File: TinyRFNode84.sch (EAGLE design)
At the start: 13 parts, among them IC3 MCP1703CB, T1 2N2222, U1 ATTINY84-20SSU

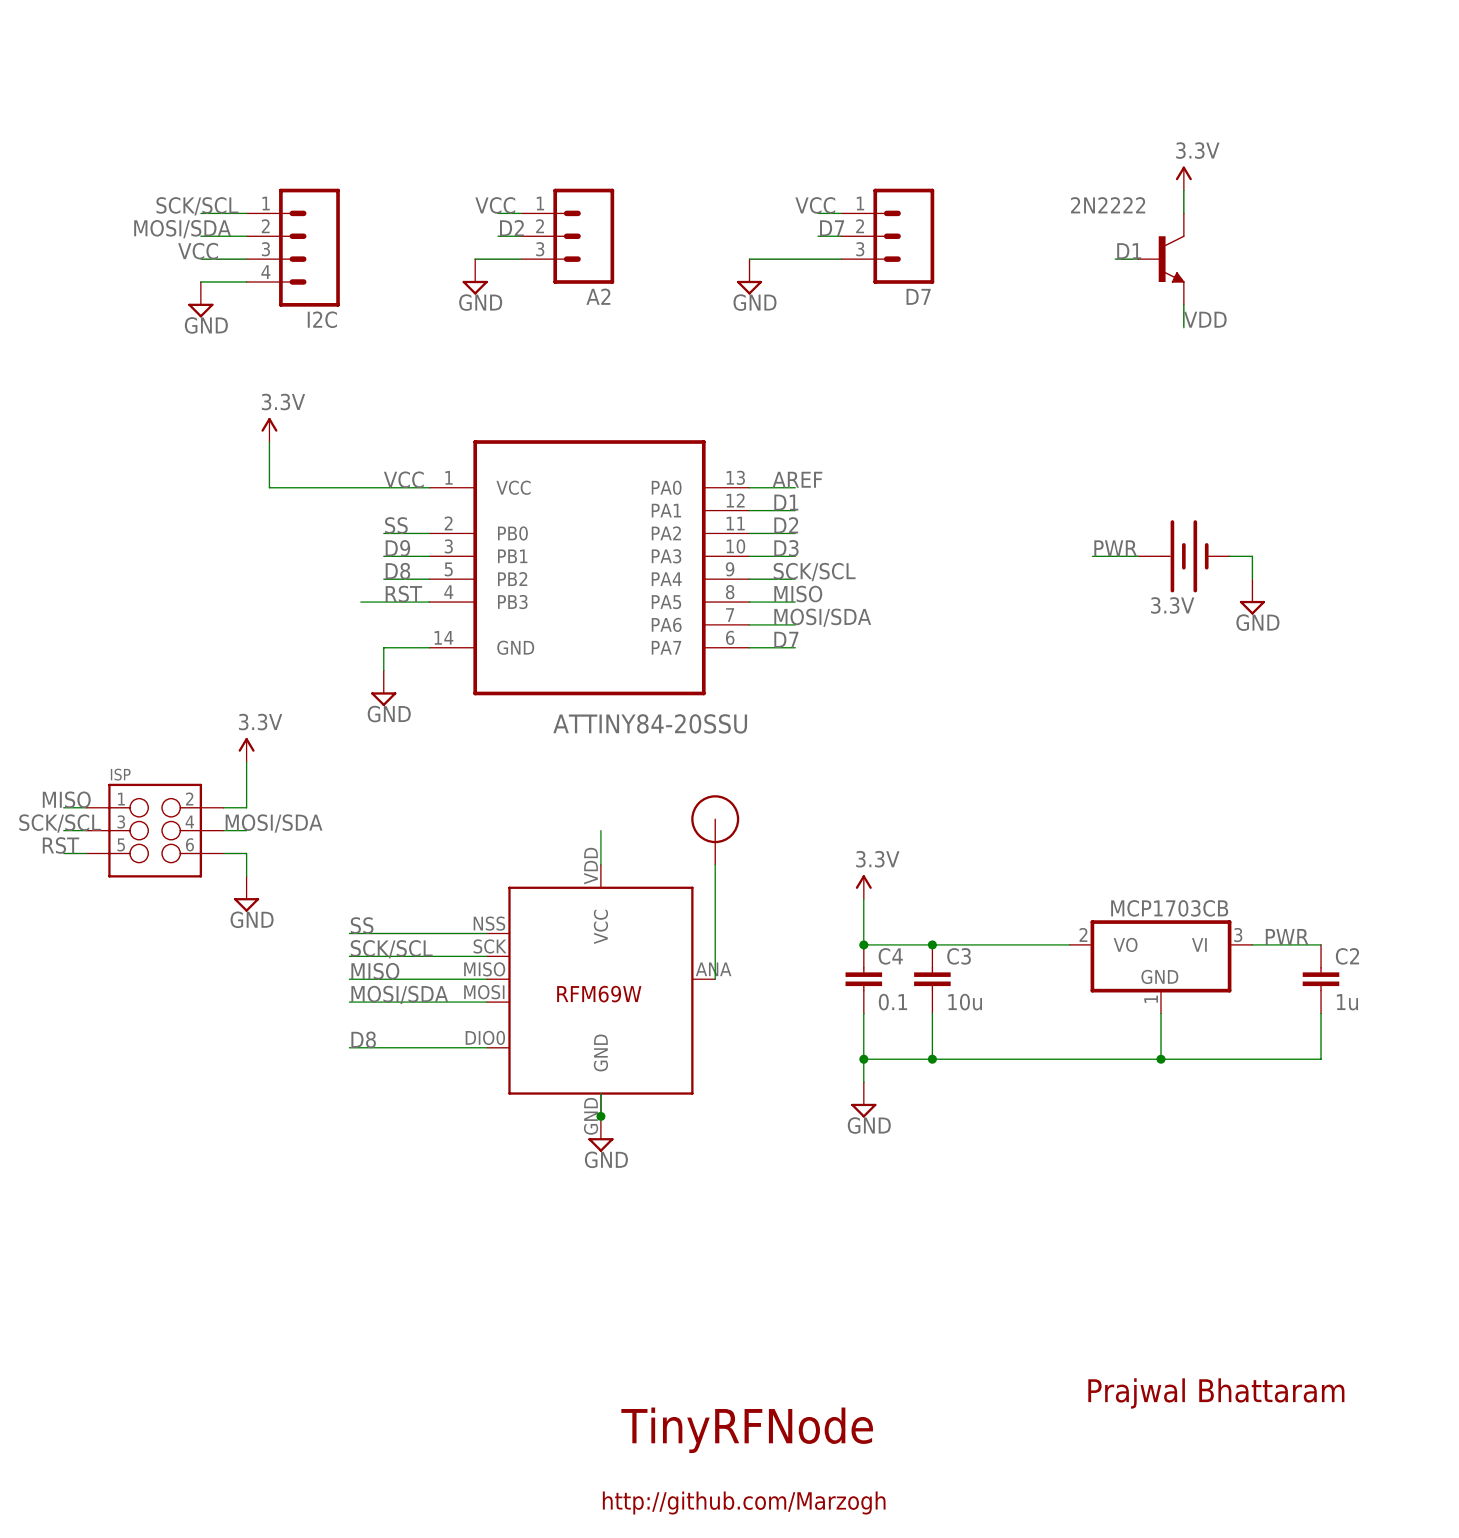
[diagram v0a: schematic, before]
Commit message: Fixed a few routing errors
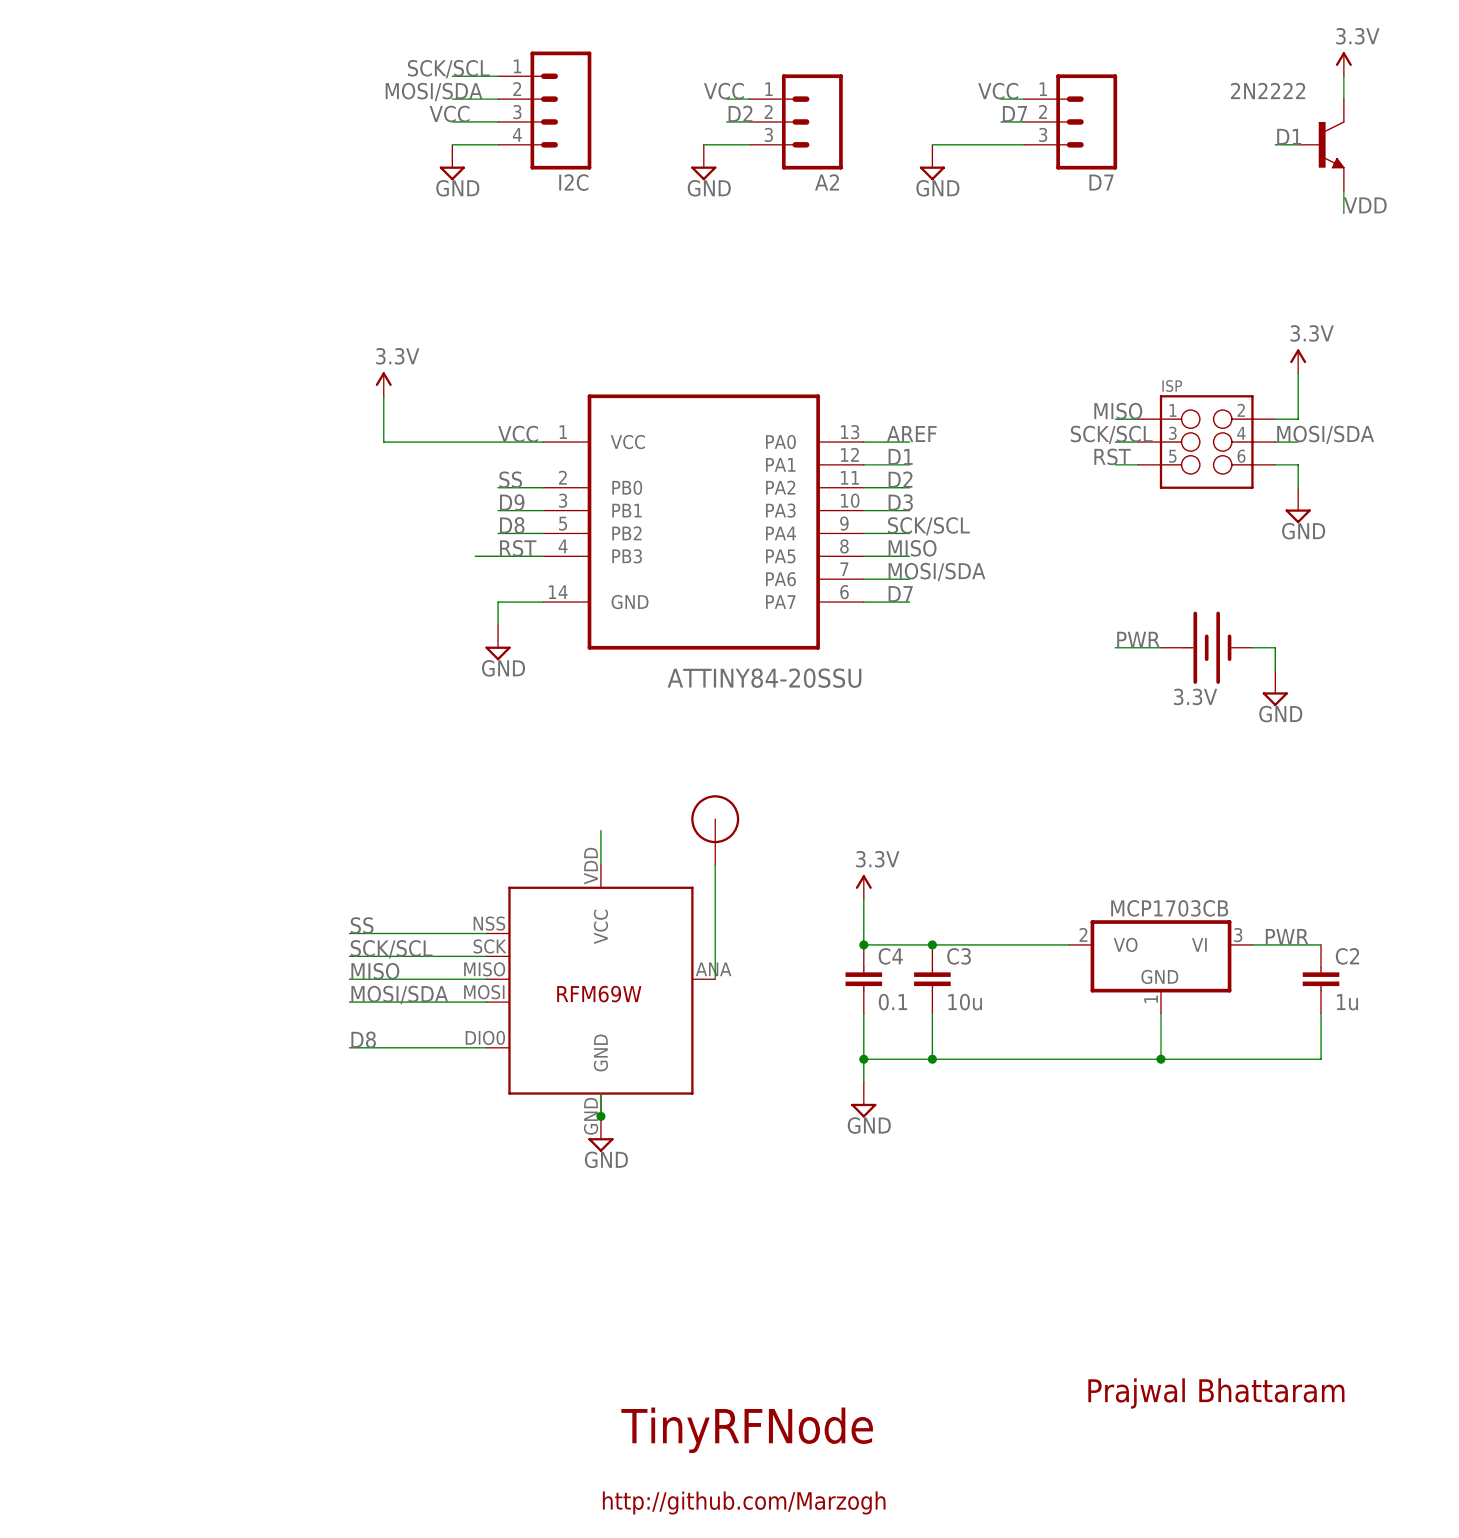
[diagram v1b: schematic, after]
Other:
- moved on the sheet: A2, D7, I2C, ISP

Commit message: v2.0.2
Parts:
- removed A2, D7: (no value), SparkFun-Connectors:M03PTH
- removed I2C: (no value), SparkFun-Connectors:M04PTH
- removed ISP: (no value), SparkFun-Connectors:M03X2FEMALE_SMD
- removed T1: 2N2222, adafruit:2N2222
- added D1: RED, SparkFun-LED:LED-RED0603
- added D2: GREEN, SparkFun-LED:LED-GREEN0603
- added D3, D4: MBRA140, SparkFun-DiscreteSemi:DIODE-SCHOTTKY-MBRA140
- added ICSP: ICSP, SparkFun-Connectors:M06NO_SILK
- added JP1: M09, SparkFun-Connectors:M09
- added JP2, JP3: M02PTH, SparkFun-Connectors:M02PTH
- added Q1: MOSFET-NCHANNELBSS138, SparkFun-DiscreteSemi:MOSFET-NCHANNELBSS138
- added R1, R2: 220, SparkFun-Passives:RESISTOR0603-RES
- added R3: 4k7, SparkFun-Passives:RESISTOR0402-RES
- added S1: RESET, SparkFun-Electromechanical:TAC_SWITCHSMD
- BAT1: device SparkFun-Electromechanical:BATTERY20SMD -> SparkFun-Electromechanical:BATTERY12MM
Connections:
- net D8 renamed D8/INT0
- removed net AREF: U1.PA0
- removed net D1: T1.B, U1.PA1
- removed net D2: A2.2, U1.PA2
- removed net D3: U1.PA3
- removed net D7: D7.2, U1.PA7
- removed net SS: U$5.SEL, U1.PB0
- removed net VDD: T1.E, U$5.VCC
- new net 3V: C2.1, D3.C, D4.C, IC3.VI
- new net BAT: BAT1.+, D3.A
- new net D0/A0/AREF: JP1.9, U1.PA0
- new net D1/A1: JP1.8, Q1.G, U1.PA1
- new net D10/SS: R1.2, U$5.SEL, U1.PB0
- new net D2/A2: JP1.7, U1.PA2
- new net D3/A3: JP1.6, U1.PA3
- new net D7/A7: JP1.2, U1.PA7
- new net N$12: D1.A, R2.1
- new net N$13: D2.A, R1.1
- new net SW_GND: D1.C, D2.C, JP3.1, Q1.S, U$5.GND
- net D9: now also JP1.1, R2.2
- net GND: now also ICSP.5, JP2.1, Q1.D, S1.1; no longer A2.3, D7.3, I2C.4, ISP.6, U$5.GND
- net MISO: now also ICSP.3, JP1.4; no longer ISP.1
- net MOSI/SDA: now also ICSP.6, JP1.3; no longer I2C.2, ISP.4
- net PWR: now also D4.A, JP2.2; no longer BAT1.+, C2.1, IC3.VI
- net RST: now also ICSP.1, R3.1, S1.3; no longer ISP.5
- net SCK/SCL: now also ICSP.2, JP1.5; no longer I2C.1, ISP.3
- net VCC: now also ICSP.4, JP3.2, R3.2, U$5.VCC; no longer A2.1, D7.1, I2C.3, ISP.2, T1.C
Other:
- moved on the sheet: C2, C3, C4
